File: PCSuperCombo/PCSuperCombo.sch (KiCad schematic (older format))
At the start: 23 parts, among them J1 IDE to CF adapter, J2 CF Adapter Power, J3 Bus_ISA_8bit, SW1 Options, U1 BIOS FLASH, U2 74HCT245, U3 ATF/GAL16V8x-15, U4 DS1315, Y1 32.768 KHz

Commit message: PCSuperCombo: Early WIP.
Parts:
- removed SW1: Options, Button_Switch_THT:SW_DIP_SPSTx04_Slide_9.78x12.34mm_W7.62mm_P2.54mm, symbol Switch:SW_DIP_x04
- added C6, C7: 0.1uF, Capacitor_SMD:C_1206_3216Metric, symbol Device:C
- added C9: 10uf 16v, Capacitor_Tantalum_SMD:CP_EIA-3216-18_Kemet-A, symbol Device:CP
- added R4, R5, R6, R7, R8: 10K, Resistor_SMD:R_1206_3216Metric, symbol Device:R
- added SW1: SW_DIP_x10, Button_Switch_THT:SW_DIP_SPSTx10_Slide_9.78x27.58mm_W7.62mm_P2.54mm, symbol Switch:SW_DIP_x10
- added U5, U6: AS6C1/4008-55PCN, Package_DIP:DIP-32_W15.24mm_Socket, symbol Memory_RAM:AS6C4008-55PCN
- added U7: ATF/GAL16V8x-15, Package_DIP:DIP-24_W7.62mm_Socket, symbol 00Common:GAL16V8
- BAT1: LCSC C964748 -> (none); Part options C964748, C964751, C964750 -> (none)
- C8: renamed from C6; value 22-44uF 16-25v -> 10uf 16v; footprint Capacitor_Tantalum_SMD:CP_EIA-3528-15_AVX-H -> Capacitor_Tantalum_SMD:CP_EIA-3216-18_Kemet-A; LCSC C10785 -> C7171; Part options C10785, C125779, C139576 -> (none)
- J1: value IDE to CF adapter -> IDE_CONNECTOR; LCSC C35165 -> (none)
- J2: LCSC C225499 -> (none); Part options C225499, C49661 -> (none)
- U1: LCSC C146583 -> (none); Part options C72122, C146583, C2331 -> (none)
- U2: LCSC C72118 -> (none); Part options C72118, C132507, C2328 -> (none)
- U3: footprint Package_DIP:DIP-20_W7.62mm_Socket -> Package_DIP:DIP-24_W7.62mm_Socket; LCSC C72118 -> (none); Part options C72118, C132507, C2328 -> (none)
- U4: LCSC C72115 -> (none); Part options C72115, C146580, C2326 -> (none)
- Y1: LCSC C127496 -> (none)
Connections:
- net labels added: BASE_RAM_0, BASE_RAM_1, BASE_RAM_2, UBM_SIZE, UMB_ENABLE, ~CARD_SEL, ~CARD_SEL_ISA, ~CE~_BIOS, ~IOR_OR_MEMR, ~IOR~_DELAYED, ~MEMR~_DELAYED
- net labels removed: AEN
- wire segments 117 -> 143
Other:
- note added: "128Kx8 for UMB only\nwhen all of 512Kx8\nneeded for base."
- note added: "512Kx8 for base + UMB\n128Kx8 OK for UMB only"
- note added: "SRAM"
- moved on the sheet: C1, C8, U1, U2

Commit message: PCSuperCombo: Early layout work.
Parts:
- added C8: 0.1uF, Capacitor_SMD:C_1206_3216Metric, symbol Device:C
- U3, U7: footprint Package_DIP:DIP-24_W7.62mm_Socket -> Package_DIP:DIP-20_W7.62mm_Socket
- renumbered C9 to C10, C8 to C9
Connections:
- net GND: now also C8.2
- net VCC: now also C8.1
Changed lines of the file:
@@
 F 0 "U3" H 4650 2450 50  0000 C CNN
 F 1 "ATF/GAL16V8x-15" H 4900 2350 50  0000 C CNN
-F 2 "Package_DIP:DIP-24_W7.62mm_Socket" H 4450 1700 50  0001 C CNN
+F 2 "Package_DIP:DIP-20_W7.62mm_Socket" H 4450 1700 50  0001 C CNN
 F 3 "" H 4450 1700 50  0001 C CNN
 	1    4450 1700
@@
 $EndComp
 $Comp
-L Device:CP C8
+L Device:CP C9
 U 1 1 60440B68
 P 5050 7850
-F 0 "C8" H 5168 7896 50  0000 L CNN
+F 0 "C9" H 5168 7896 50  0000 L CNN
 F 1 "10uf 16v" H 4900 7400 50  0000 L CNN
 F 2 "Capacitor_Tantalum_SMD:CP_EIA-3216-18_Kemet-A" H 5088 7700 50  0001 C CNN
@@
 $EndComp
 $Comp
-L Device:CP C9
+L Device:CP C10
 U 1 1 61625895
 P 5500 7850
-F 0 "C9" H 5618 7896 50  0000 L CNN
+F 0 "C10" H 5618 7896 50  0000 L CNN
 F 1 "10uf 16v" H 5350 7400 50  0000 L CNN
 F 2 "Capacitor_Tantalum_SMD:CP_EIA-3216-18_Kemet-A" H 5538 7700 50  0001 C CNN
@@
 F 0 "U7" H 4650 4400 50  0000 C CNN
 F 1 "ATF/GAL16V8x-15" H 4900 4300 50  0000 C CNN
-F 2 "Package_DIP:DIP-24_W7.62mm_Socket" H 4450 3650 50  0001 C CNN
+F 2 "Package_DIP:DIP-20_W7.62mm_Socket" H 4450 3650 50  0001 C CNN
 F 3 "" H 4450 3650 50  0001 C CNN
 	1    4450 3650
@@
 	1    0    0    -1
 $EndComp
+$Comp
+L power:VCC #PWR?
+U 1 1 6167D171
+P 4200 7800
+F 0 "#PWR?" H 4200 7650 50  0001 C CNN
+F 1 "VCC" H 4215 7973 50  0000 C CNN
+F 2 "" H 4200 7800 50  0001 C CNN
+F 3 "" H 4200 7800 50  0001 C CNN
+	1    4200 7800
+	1    0    0    -1
+$EndComp
+$Comp
+L power:GND #PWR?
+U 1 1 6167D911
+P 4200 8100
+F 0 "#PWR?" H 4200 7850 50  0001 C CNN
+F 1 "GND" H 4205 7927 50  0000 C CNN
+F 2 "" H 4200 8100 50  0001 C CNN
+F 3 "" H 4200 8100 50  0001 C CNN
+	1    4200 8100
+	1    0    0    -1
+$EndComp
+$Comp
+L Device:C C8
+U 1 1 6167D91D
+P 4200 7950
+F 0 "C8" H 4315 7996 50  0000 L CNN
+F 1 "0.1uF" H 4315 7905 50  0000 L CNN
+F 2 "Capacitor_SMD:C_1206_3216Metric" H 4238 7800 50  0001 C CNN
+F 3 "~" H 4200 7950 50  0001 C CNN
+F 4 " C24497" H 4200 7950 50  0001 C CNN "LCSC"
+F 5 "" H 4200 7950 50  0001 C CNN "Part options"
+	1    4200 7950
+	1    0    0    -1
+$EndComp

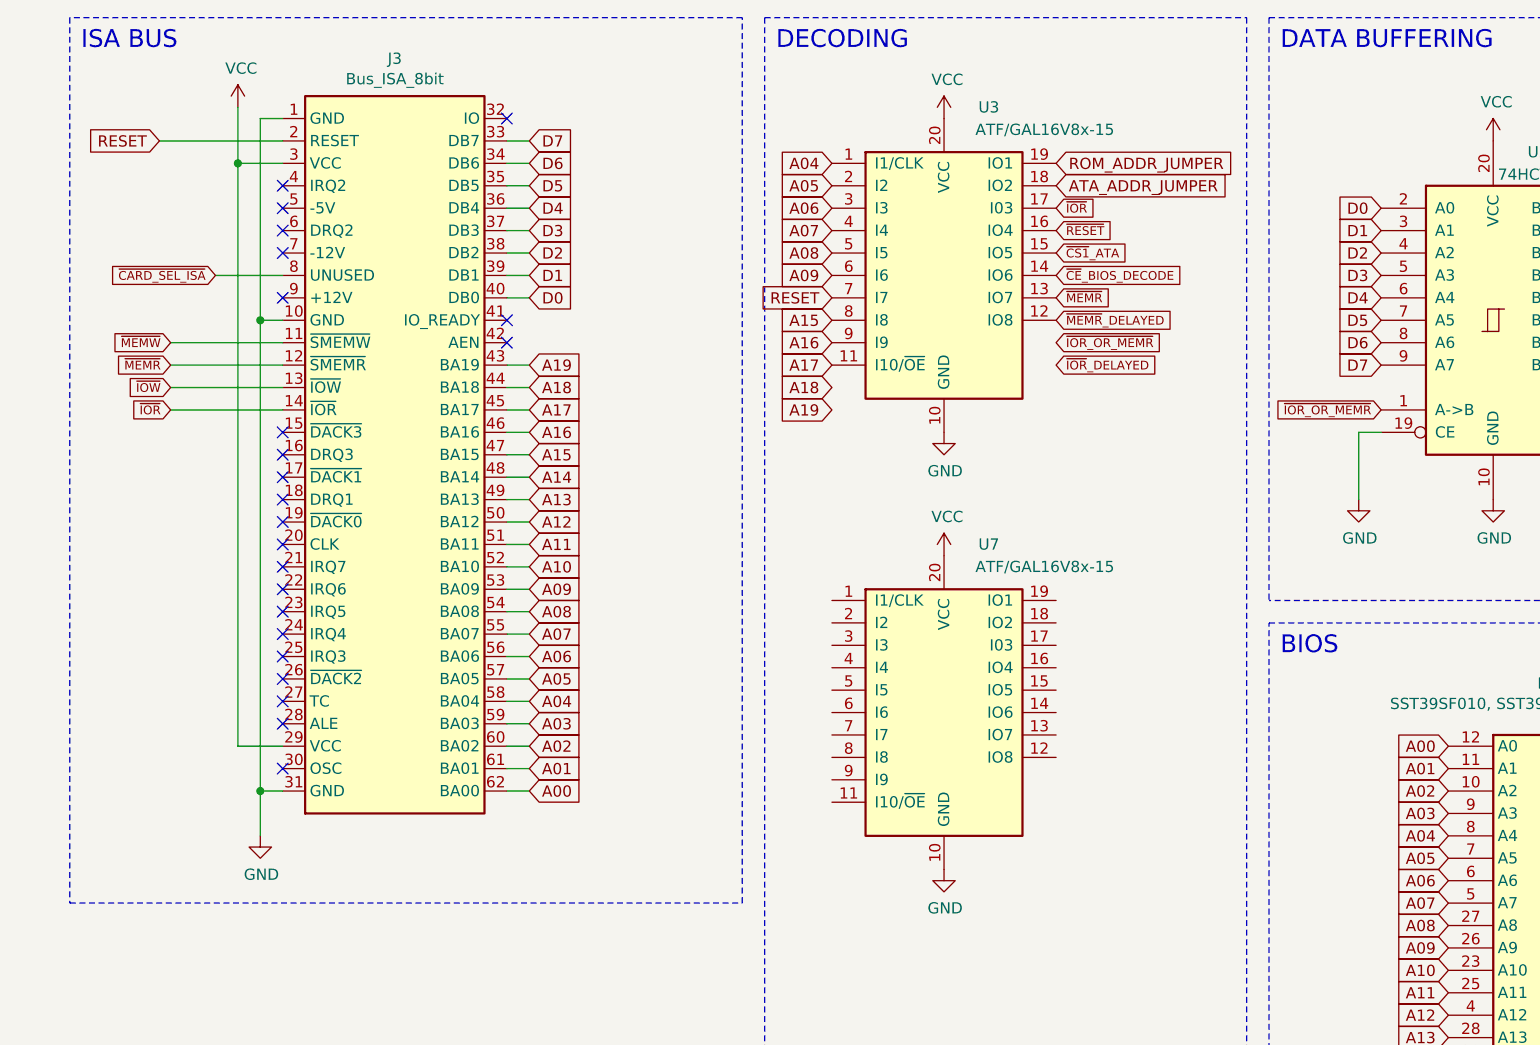
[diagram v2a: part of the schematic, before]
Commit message: PCSuperCombo: Some layout experiments. Schematic needs to be completed before proceeding further.
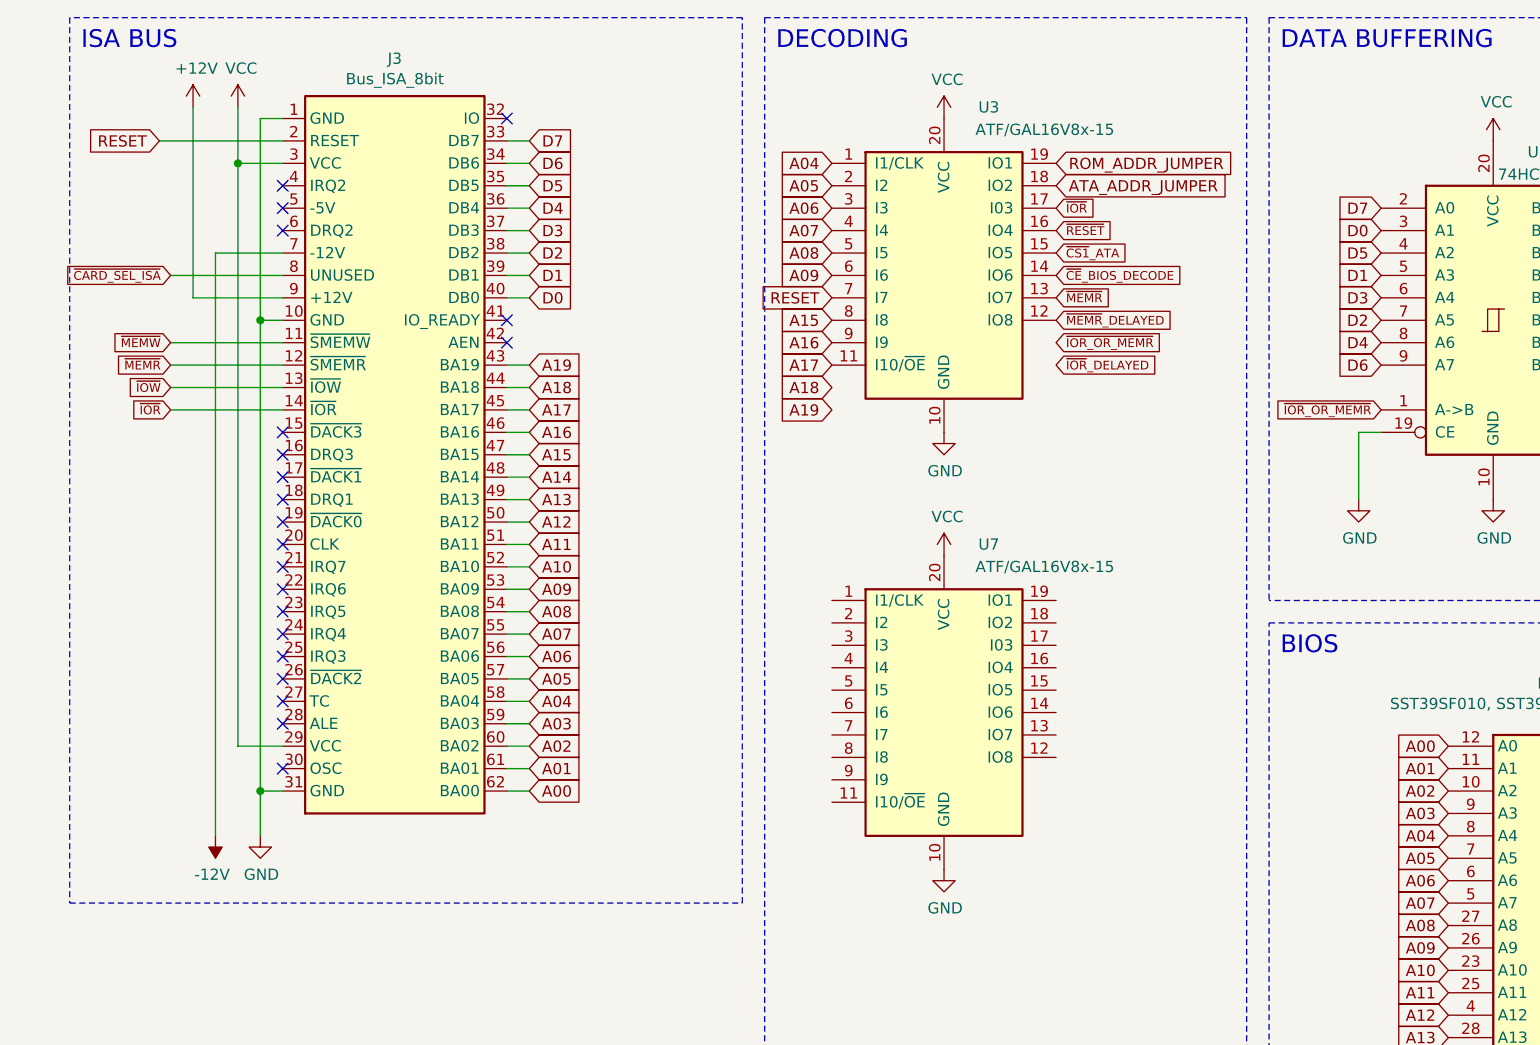
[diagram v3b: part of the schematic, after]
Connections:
- net D0: now also U2.3 (A1); no longer U2.2 (A0)
- net D1: now also U2.5 (A3); no longer U2.3 (A1)
- net D2: now also U2.7 (A5); no longer U2.4 (A2)
- net D3: now also U2.6 (A4); no longer U2.5 (A3)
- net D4: now also U2.8 (A6); no longer U2.6 (A4)
- net D5: now also U2.4 (A2); no longer U2.7 (A5)
- net D6: now also U2.9 (A7); no longer U2.8 (A6)
- net D7: now also U2.2 (A0); no longer U2.9 (A7)
- net -12V: now reaches J3.7 (-12V)
- net +12V: now reaches J3.9 (+12V)
- no-connect marks 38 -> 36
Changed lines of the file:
@@
 NoConn ~ 2500 2000
 NoConn ~ 1500 1400
-NoConn ~ 1500 1600
-NoConn ~ 1500 1800
 Wire Wire Line
 	9950 2750 10400 2750
@@
 Text GLabel 7400 1400 2    50   Input ~ 0
 D0_BUF
+Text GLabel 6400 1400 0    50   Input ~ 0
+D7
 Text GLabel 6400 2100 0    50   Input ~ 0
-D7
+D6
+Text GLabel 6400 1600 0    50   Input ~ 0
+D5
 Text GLabel 6400 2000 0    50   Input ~ 0
-D6
+D4
+Text GLabel 6400 1800 0    50   Input ~ 0
+D3
 Text GLabel 6400 1900 0    50   Input ~ 0
-D5
-Text GLabel 6400 1800 0    50   Input ~ 0
-D4
+D2
 Text GLabel 6400 1700 0    50   Input ~ 0
-D3
-Text GLabel 6400 1600 0    50   Input ~ 0
-D2
+D1
 Text GLabel 6400 1500 0    50   Input ~ 0
-D1
-Text GLabel 6400 1400 0    50   Input ~ 0
 D0
 Text GLabel 6400 2300 0    39   Input ~ 0
@@
 Text GLabel 4950 1800 2    39   Input ~ 0
 ~MEMR
-$Comp
-L 00Common:Bus_ISA_8bit J3
-U 1 1 6039F90B
-P 2000 2500
-F 0 "J3" H 2000 4267 50  0000 C CNN
-F 1 "Bus_ISA_8bit" H 2000 4176 50  0000 C CNN
-F 2 "00Custom:BUS_XT" H 2000 2500 50  0001 C CNN
-F 3 "https://en.wikipedia.org/wiki/Industry_Standard_Architecture" H 2000 2500 50  0001 C CNN
-	1    2000 2500
-	1    0    0    -1
-$EndComp
 Text Label 2500 6300 0    50   ~ 0
 XTAL2
@@
 Text GLabel 12650 2350 2    39   Input ~ 0
 ~CARD_SEL_ISA
-Text GLabel 1200 1700 0    39   Input ~ 0
+Text GLabel 1000 1700 0    39   Input ~ 0
 ~CARD_SEL_ISA
 Wire Wire Line
-	1500 1700 1200 1700
+	1500 1700 1000 1700
 Text GLabel 13900 1450 2    50   Input ~ 0
 BASE_RAM_0
@@
 $EndComp
 $Comp
-L power:VCC #PWR?
+L power:VCC #PWR0153
 U 1 1 6167D171
 P 4200 7800
-F 0 "#PWR?" H 4200 7650 50  0001 C CNN
+F 0 "#PWR0153" H 4200 7650 50  0001 C CNN
 F 1 "VCC" H 4215 7973 50  0000 C CNN
 F 2 "" H 4200 7800 50  0001 C CNN
@@
 $EndComp
 $Comp
-L power:GND #PWR?
+L power:GND #PWR0154
 U 1 1 6167D911
 P 4200 8100
-F 0 "#PWR?" H 4200 7850 50  0001 C CNN
+F 0 "#PWR0154" H 4200 7850 50  0001 C CNN
 F 1 "GND" H 4205 7927 50  0000 C CNN
 F 2 "" H 4200 8100 50  0001 C CNN
@@
 	1    0    0    -1
 $EndComp
+$Comp
+L 00Common:Bus_ISA_8bit J3
+U 1 1 6039F90B
+P 2000 2500
+F 0 "J3" H 2000 4267 50  0000 C CNN
+F 1 "Bus_ISA_8bit" H 2000 4176 50  0000 C CNN
+F 2 "00Custom:BUS_XT" H 2000 2500 50  0001 C CNN
+F 3 "https://en.wikipedia.org/wiki/Industry_Standard_Architecture" H 2000 2500 50  0001 C CNN
+	1    2000 2500
+	1    0    0    -1
+$EndComp
+Wire Wire Line
+	1500 1800 1100 1800
+Wire Wire Line
+	1100 1800 1100 950
+Wire Wire Line
+	1500 1600 1200 1600
+Wire Wire Line
+	1200 1600 1200 4200
+$Comp
+L power:+12V #PWR0155
+U 1 1 616413D9
+P 1100 950
+F 0 "#PWR0155" H 1100 800 50  0001 C CNN
+F 1 "+12V" H 1115 1123 50  0000 C CNN
+F 2 "" H 1100 950 50  0001 C CNN
+F 3 "" H 1100 950 50  0001 C CNN
+	1    1100 950
+	1    0    0    -1
+$EndComp
+$Comp
+L power:-12V #PWR0156
+U 1 1 616422F6
+P 1200 4200
+F 0 "#PWR0156" H 1200 4300 50  0001 C CNN
+F 1 "-12V" H 1215 4373 50  0000 C CNN
+F 2 "" H 1200 4200 50  0001 C CNN
+F 3 "" H 1200 4200 50  0001 C CNN
+	1    1200 4200
+	-1   0    0    1
+$EndComp
 $EndSCHEMATC

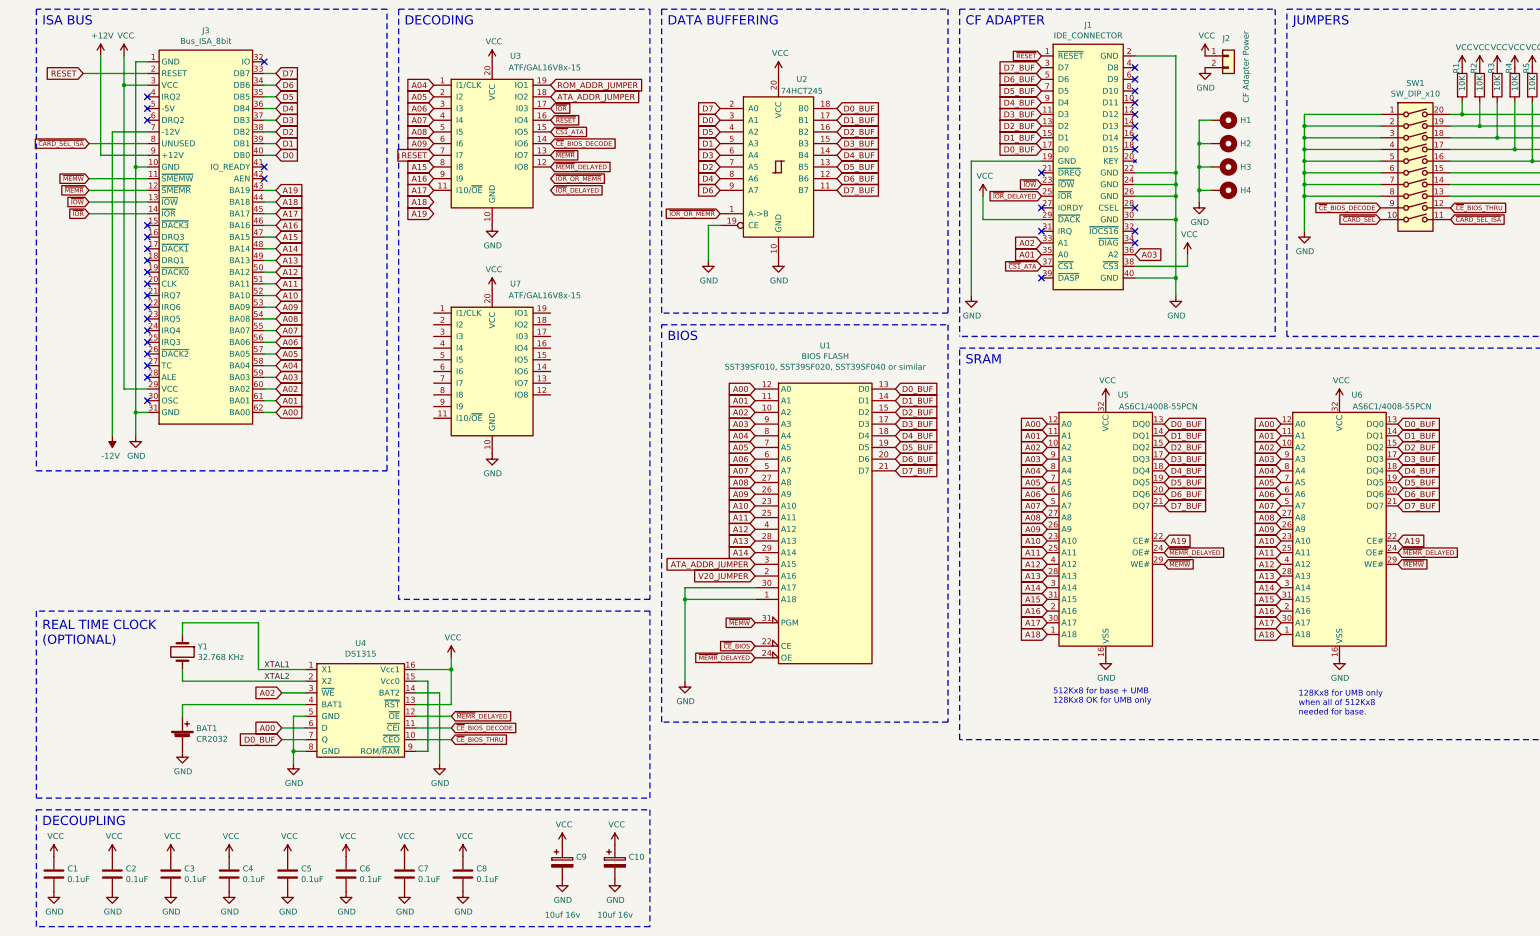
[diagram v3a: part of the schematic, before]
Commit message: PCSuperCombo: Complete glue connectons to GAL's. Add circuit for LED drive.
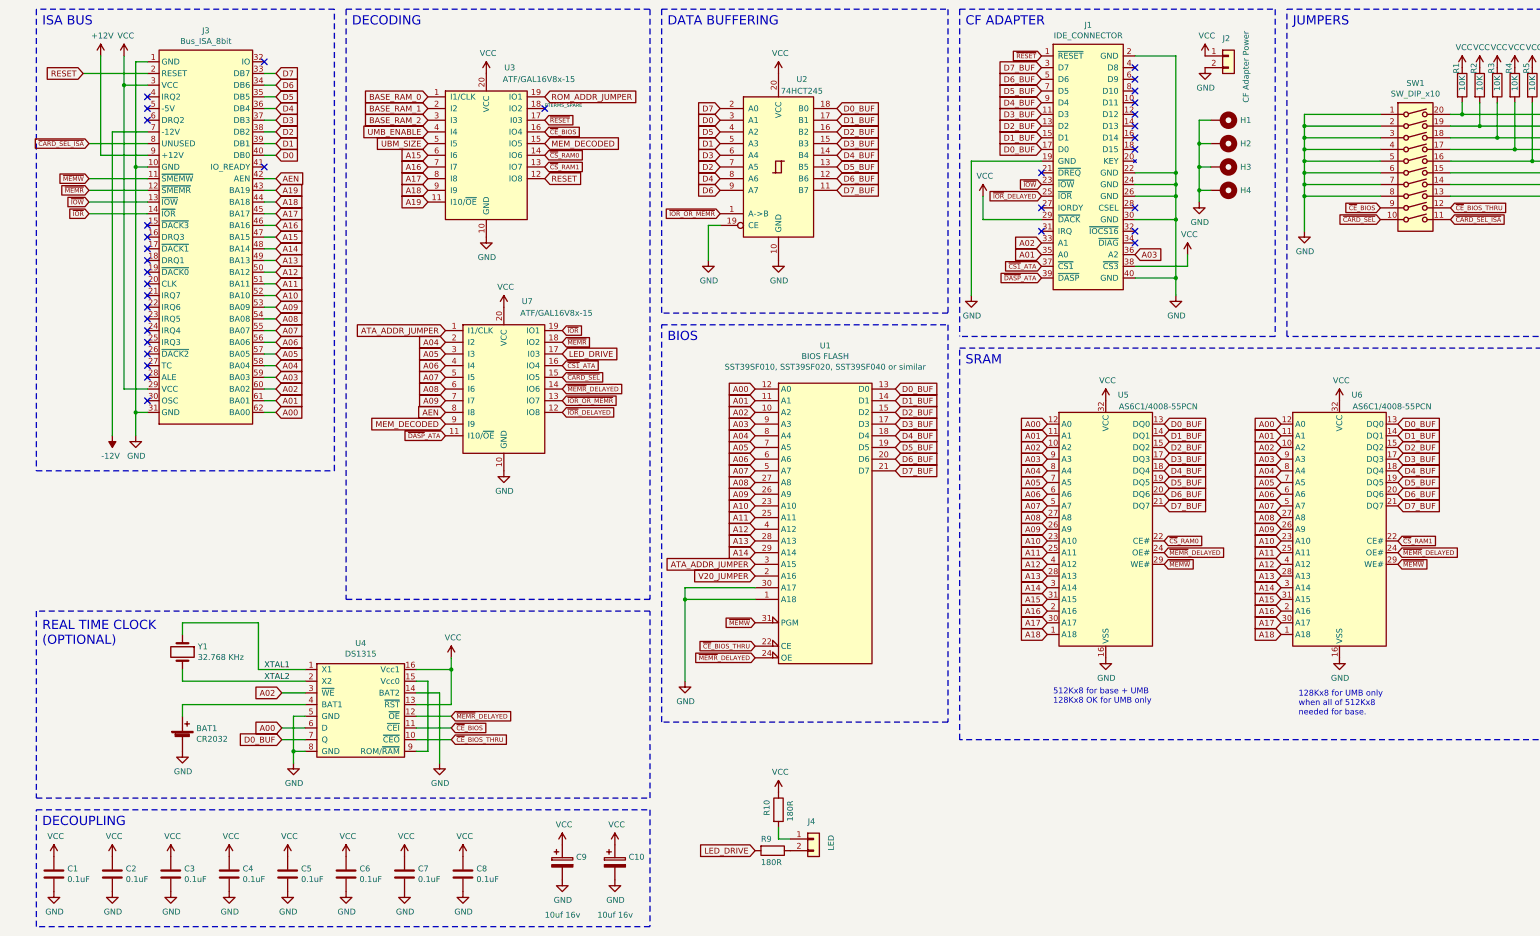
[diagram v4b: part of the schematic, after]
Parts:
- added J4: LED, Connector_PinHeader_2.54mm:PinHeader_1x02_P2.54mm_Horizontal, symbol Connector_Generic:Conn_01x02
- added R10, R9: 180R, Resistor_SMD:R_1206_3216Metric, symbol Device:R
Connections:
- net A04: now also U7.2 (I2); no longer U3.1 (I1/CLK)
- net A05: now also U7.3 (I3); no longer U3.2 (I2)
- net A06: now also U7.4 (I4); no longer U3.3 (I3)
- net A07: now also U7.5 (I5); no longer U3.4 (I4)
- net A08: now also U7.6 (I6); no longer U3.5 (I5)
- net A09: now also U7.7 (I7); no longer U3.6 (I6)
- net A15: now also U3.6 (I6); no longer U3.8 (I8)
- net A16: now also U3.7 (I7); no longer U3.9 (I9)
- net A17: now also U3.8 (I8); no longer U3.11 (I10/~OE~)
- net A18: now also U3.9 (I9)
- net A19: now also U3.11 (I10/~OE~); no longer U5.22 (CE#), U6.22 (CE#)
- net ATA_ADDR_JUMPER: now also U7.1 (I1/CLK); no longer U3.18 (IO2)
- net BASE_RAM_0: now also U3.1 (I1/CLK)
- net BASE_RAM_1: now also U3.2 (I2)
- net BASE_RAM_2: now also U3.3 (I3)
- net RESET: now also U3.12 (IO8); no longer U3.7 (I7)
- net UBM_SIZE: now also U3.5 (I5)
- net UMB_ENABLE: now also U3.4 (I4)
- net VCC: now also R10.1
- net ~CARD_SEL: now also U7.15 (IO5)
- net ~CE~_BIOS: now also SW1.9, U3.16 (IO4), U4.11 (~CEI); no longer U1.22 (CE)
- net ~CE~_BIOS_THRU: now also U1.22 (CE)
- net ~CS1~_ATA: now also U7.16 (IO4); no longer U3.15 (IO5)
- net ~IOR: now also U7.19 (IO1); no longer U3.17 (I03)
- net ~IOR_OR_MEMR: now also U7.13 (IO7)
- net ~IOR~_DELAYED: now also U7.12 (IO8)
- net ~MEMR: now also U7.18 (IO2); no longer U3.13 (IO7)
- net ~MEMR~_DELAYED: now also U7.14 (IO6); no longer U3.12 (IO8)
- net ~RESET: now also U3.17 (I03); no longer U3.16 (IO4)
- net AEN: now reaches J3.42 (AEN)
- net AEN: now also U7.8 (I8)
- net ~DASP~_ATA: now reaches J1.39 (~DASP)
- net ~DASP~_ATA: now also U7.11 (I10/~OE~)
- net LED_DRIVE: now reaches U7.17 (I03)
- net LED_DRIVE: now also R9.2
- net MEM_DECODED: now reaches U7.9 (I9)
- net MEM_DECODED: now also U3.15 (IO5)
- removed net ~CE~_BIOS_DECODE: SW1.9, U3.14 (IO6), U4.11 (~CEI)
- new net: J4.1 (Pin_1), R10.2
- new net: J4.2 (Pin_2), R9.1
- new net PTERMS_SPARE: U3.18 (IO2)
- new net ~CS~_RAM0: U3.14 (IO6), U5.22 (CE#)
- new net ~CS~_RAM1: U3.13 (IO7), U6.22 (CE#)
- no-connect marks 36 -> 35
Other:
- moved on the sheet: U3, U7
